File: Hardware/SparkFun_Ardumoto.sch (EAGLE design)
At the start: 33 parts, among them U1 ARDUINO, U2 L298, U3 74HC1G04, U4 74HC1G04

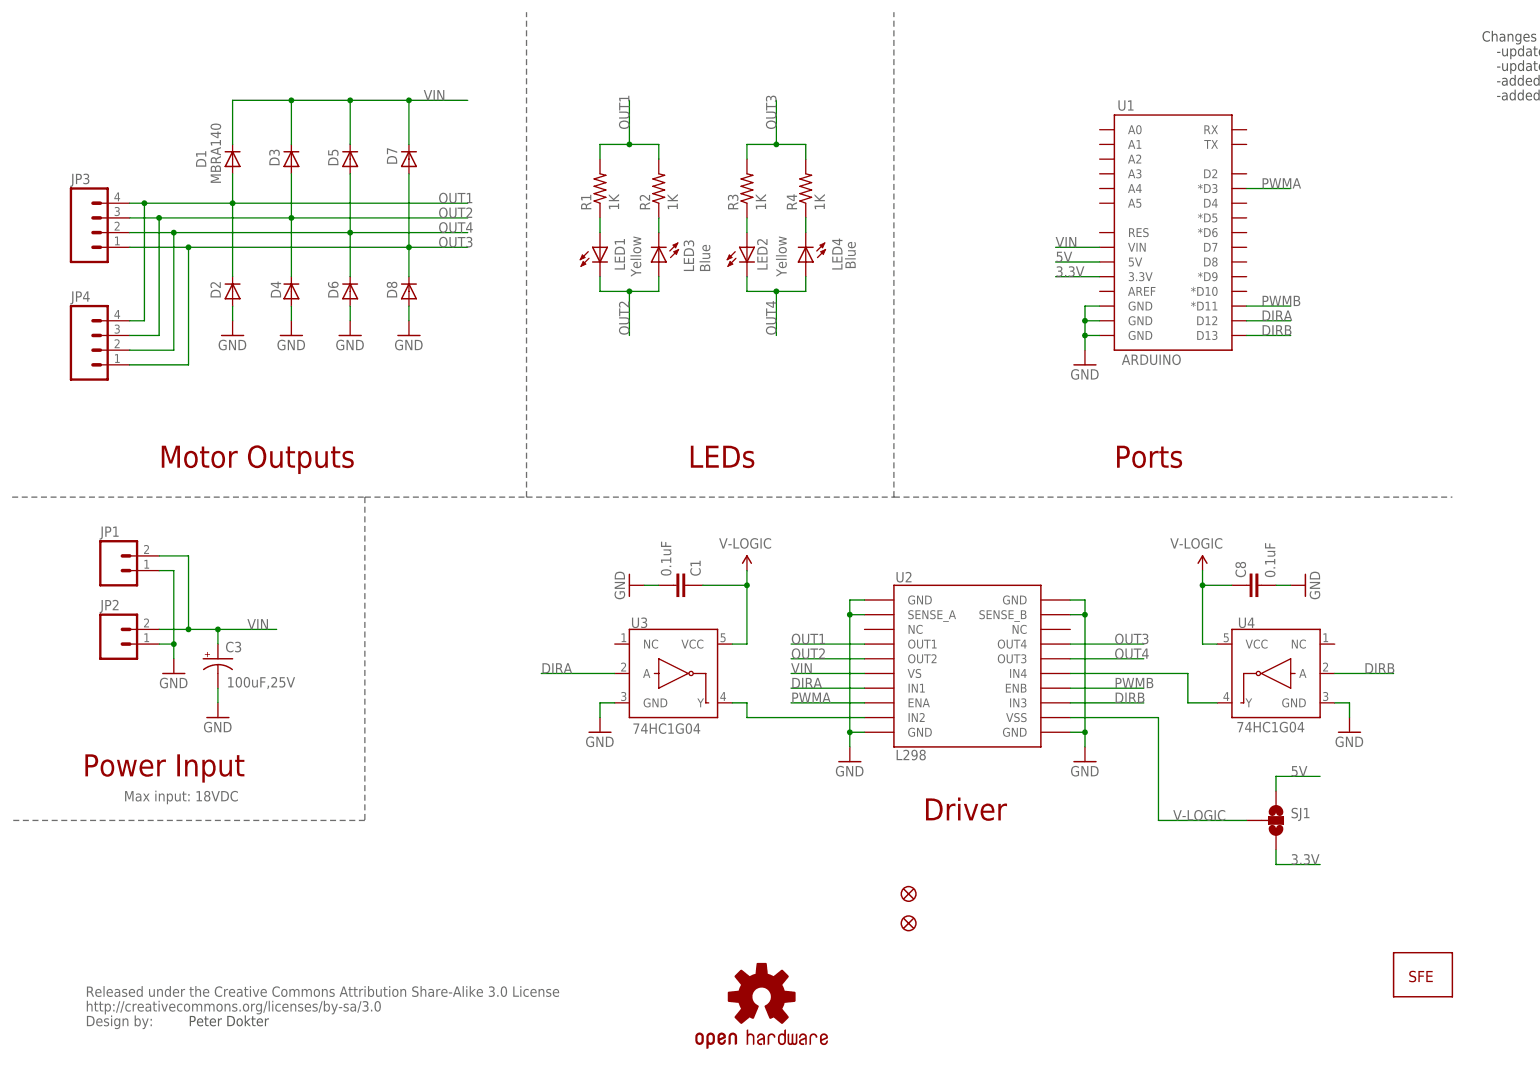
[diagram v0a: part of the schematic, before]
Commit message: Schematic is the same, but all parts have been updated to the new libraries.  The layout is no longer valid, and proto area has been moved aside.  This is ready for functional changes.
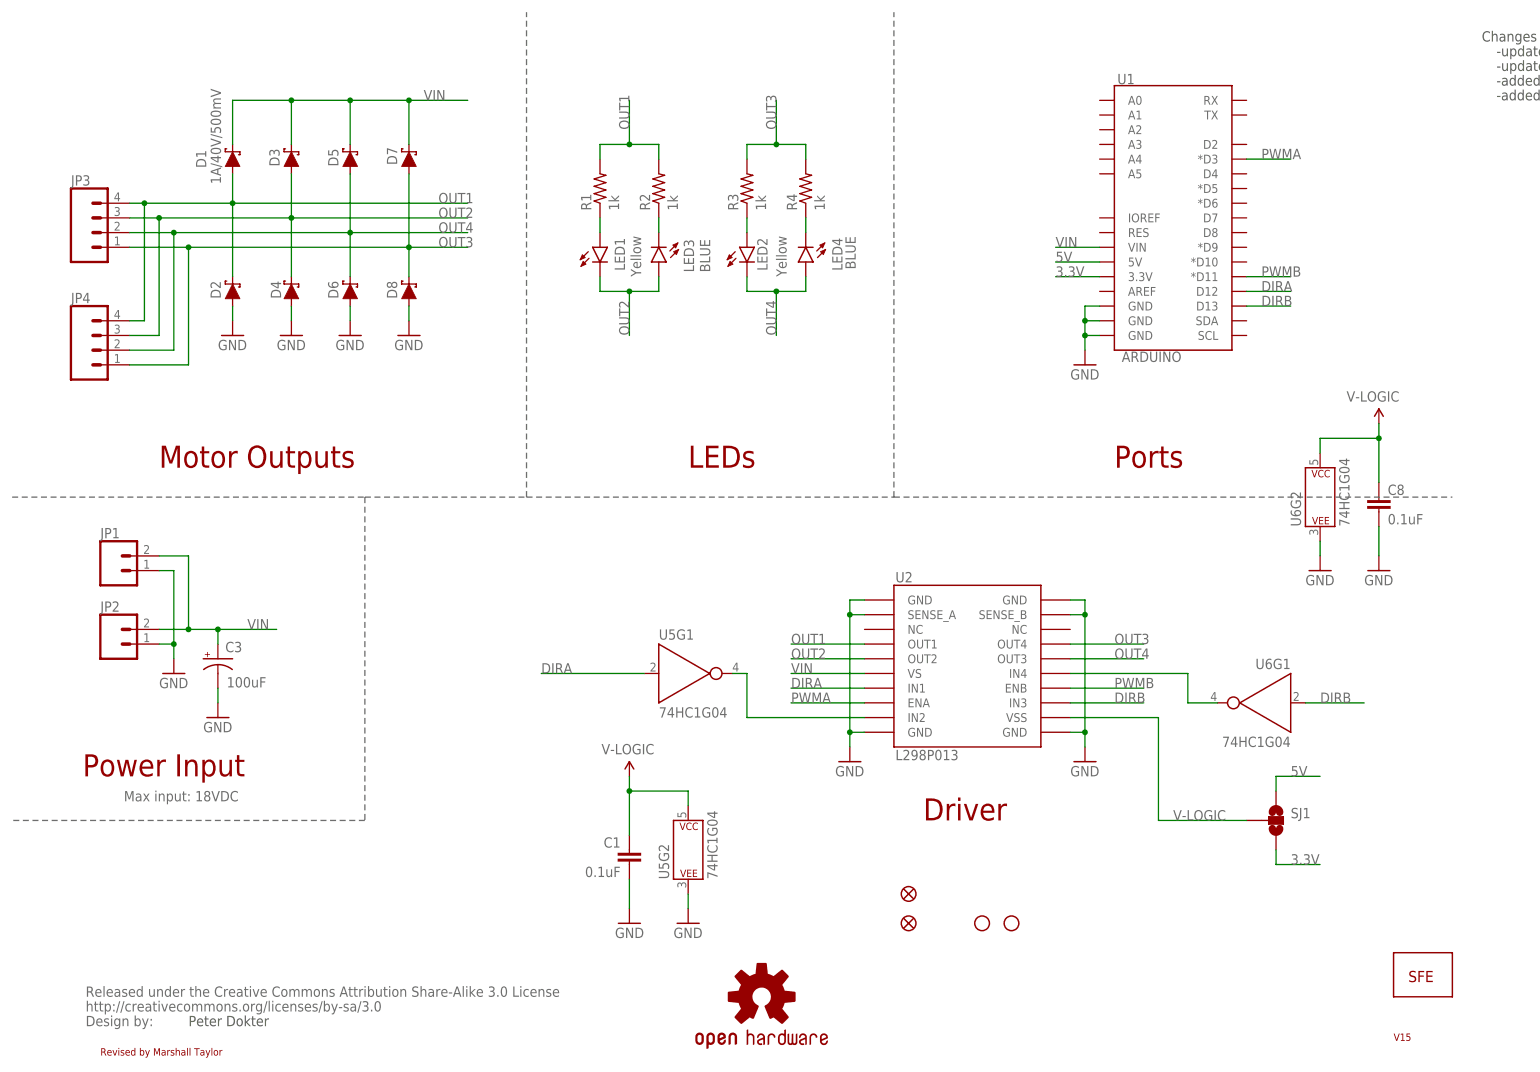
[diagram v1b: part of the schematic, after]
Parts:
- removed U3, U4: 74HC1G04, SparkFun:INVERTER""
- added H1, H2: STAND-OFF, SparkFun-Hardware:STAND-OFF
- added U5, U6: 74HC1G04, SparkFun-IC-Logic:74HC1G04
- C1, C8: device SparkFun:CAP0402-CAP -> SparkFun-Capacitors:0.1UF-0603-25V-5%
- C3: value 100uF,25V -> 100uF; device SparkFun:CAP_POLF80 -> SparkFun-Capacitors:100UF-POLAR-25V-20%(ELEC)
- D1, D2, D3, D4, D5, D6, D7, D8: value MBRA140 -> 1A/40V/500mV; device SparkFun:DIODESMA -> SparkFun-DiscreteSemi:DIODE-SCHOTTKY-SS14
- JP1: device SparkFun:M02PTH -> SparkFun-Connectors:CONN_02
- JP2: device SparkFun:M023.5MM -> SparkFun-Connectors:CONN_023.5MM
- JP3: device SparkFun:M04SCREW -> SparkFun-Connectors:CONN_04SCREW
- JP4: device SparkFun:M04PTH -> SparkFun-Connectors:CONN_04
- LED1, LED2: device SparkFun:LED0603 -> SparkFun-LED:LED-YELLOW0603
- LED3, LED4: value Blue -> BLUE; device SparkFun:LED0603 -> SparkFun-LED:LED-BLUE0603
- R1, R2, R3, R4: value 1K -> 1k; device SparkFun:RESISTOR0402-RES -> SparkFun-Resistors:1KOHM-0603-1/10W-1%
- U1: device SparkFun:ARDUINO_SHIELDNOLABELS -> SparkFun-Boards:ARDUINO_UNO_R3_SHIELDBASIC
- U2: value L298 -> L298P013; device SparkFun:L298_BRIDGE_DRIVER -> SparkFun-IC-Special-Function:L298_BRIDGE_DRIVER
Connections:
- net DIRA: now also U5G1.A; no longer U3.A
- net DIRB: now also U6G1.A; no longer U4.A
- net GND: now also U6G2.P$V-; no longer U3.GND, U4.GND
- net N$1: now also U5G1.Y; no longer U3.Y
- net N$2: now also U6G1.Y; no longer U4.Y
- net V-LOGIC: now also U6G2.P$V+; no longer U3.VCC, U4.VCC
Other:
- note added: "Revised by Marshall Taylor"
- note added: "V15"
- moved on the sheet: C1, C8

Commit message: Schematic changes applied, layout is now mostly ripped up
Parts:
- removed SJ1: (no value), SparkFun:SOLDERJUMPER_2WAYPASTE1&2
- added D10, D11, D12, D9: RED, SparkFun-LED:LED-RED0603
- added J1: (no value), SparkFun-Connectors:CONN_08NO_SILK_FEMALE_PTH
- added J2, J6: (no value), SparkFun-Connectors:CONN_01PTH_NO_SILK_YES_STOP
- added J3, J5: (no value), SparkFun-Connectors:CONN_06NO_SILK_FEMALE_PTH
- added J4: (no value), SparkFun-Connectors:CONN_07NO_SILK
- added J7, J8: (no value), SparkFun-Connectors:CONN_021X02_NO_SILK
- added JP10, JP7, JP8, JP9: JUMPER-SMT_3_1-NC_TRACE_SILK, SparkFun-Jumpers:JUMPER-SMT_3_1-NC_TRACE_SILK
- added JP11, JP12: JUMPER-SMT_2_NC_TRACE_SILK, SparkFun-Jumpers:JUMPER-SMT_2_NC_TRACE_SILK
- added R5, R6, R7, R8: 1k, SparkFun-Resistors:1KOHM-0603-1/10W-1%
- U1: device SparkFun-Boards:ARDUINO_UNO_R3_SHIELDBASIC -> SparkFun-Boards:ARDUINO_UNO_R3_SHIELDNOLABELS
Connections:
- net N$1 renamed IN2
- net N$2 renamed IN4
- removed net V-LOGIC: C1.1, C8.1, SJ1.2, U2.VSS, U6G2.P$V+
- new net D0: J1.1, U1.RX
- new net D1: J1.2, U1.TX
- new net D10: J5.3, JP10.1, U1.*D10
- new net D11: J5.4, U1.*D11
- new net D12: J5.5, U1.D12
- new net D13: J5.6, U1.D13
- new net D2: J1.3, JP7.1, U1.D2
- new net D3: J1.4, JP8.1, U1.*D3
- new net D4: J1.5, U1.D4
- new net D5: J1.6, JP9.3, U1.*D5
- new net D6: J1.7, JP9.1, U1.*D6
- new net D7: J1.8, JP7.3, U1.D7
- new net D8: J5.1, JP8.3, U1.D8
- new net D9: J5.2, JP10.3, U1.*D9
- new net IN1: J2.1, JP11.2, U2.IN1
- new net IN3: J6.1, JP12.1, U2.IN3
- new net IOREF: J4.7, U1.IOREF
- new net N$11: J8.2, U2.SENSE_B
- new net N$14: J7.1, U2.SENSE_A
- new net N$21: J3.1, U1.A0
- new net N$22: J3.2, U1.A1
- new net N$23: J3.3, U1.A2
- new net N$24: J3.4, U1.A3
- new net N$25: J3.5, U1.A4
- new net N$26: J3.6, U1.A5
- new net N$36: D9.A, R5.1
- new net N$37: D10.A, R6.1
- new net N$38: D12.A, R8.1
- new net N$39: D11.A, R7.1
- new net RESET: J4.6, U1.RES
- net 3.3V: now also J4.5; no longer SJ1.3
- net 5V: now also C1.1, C8.1, J4.4, U2.VSS, U5G2.P$V+, U6G2.P$V+; no longer SJ1.1
- net DIRA: now also JP11.1, JP8.2, R7.2; no longer U1.D12, U2.IN1
- net DIRB: now also JP12.2, JP7.2, R8.2; no longer U1.D13, U2.IN3
- net GND: now also D10.C, D11.C, D12.C, D9.C, J4.2, J4.3, J7.2, J8.1, U5G2.P$V-; no longer U2.SENSE_A, U2.SENSE_B
- net PWMA: now also JP9.2, R6.2; no longer U1.*D3
- net PWMB: now also JP10.2, R5.2; no longer U1.*D11
- net VIN: now also J4.1
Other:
- moved on the sheet: C1, C3, C8, D1, D2, D3, D4, D5, D6, D7, D8, JP1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

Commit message: Desing ready for proto 1 review
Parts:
- removed JP11, JP12: JUMPER-SMT_2_NC_TRACE_SILK, SparkFun-Jumpers:JUMPER-SMT_2_NC_TRACE_SILK
- removed U$10: LOGO-SFENEW, SparkFun:LOGO-SFENEW
- removed U$11: CREATIVE_COMMONS, SparkFun:CREATIVE_COMMONS
- added FD1, FD2: FIDUCIALUFIDUCIAL, SparkFun:FIDUCIALUFIDUCIAL
- added FRAME1: FRAME-LETTER, SparkFun-Aesthetics:FRAME-LETTER
- added FRAME2: FRAME-LETTERNO_PACKAGE, SparkFun-Aesthetics:FRAME-LETTERNO_PACKAGE
- added J10: (no value), SparkFun-Connectors:CONN_023.5MM
- added J11, J12, J13, J14: (no value), SparkFun-Connectors:CONN_01PTH_NO_SILK_YES_STOP
- added J9: (no value), SparkFun-Connectors:CONN_02
- added LOGO1: SFE_LOGO_NAME_FLAME.2_INCH, SparkFun-Aesthetics:SFE_LOGO_NAME_FLAME.2_INCH
- added LOGO2: SFE_LOGO_NAME.1_INCH, SparkFun-Aesthetics:SFE_LOGO_NAME.1_INCH
- J7: device SparkFun-Connectors:CONN_021X02_NO_SILK -> SparkFun-Connectors:CONN_04SCREW
- J8: device SparkFun-Connectors:CONN_021X02_NO_SILK -> SparkFun-Connectors:CONN_04
- JP1: value (none) -> 31NCT; device SparkFun-Connectors:CONN_02 -> SparkFun-Jumpers:JUMPER-SMT_3_1-NC_TRACE_SILK
- JP10, JP9: value JUMPER-SMT_3_1-NC_TRACE_SILK -> (none); device SparkFun-Jumpers:JUMPER-SMT_3_1-NC_TRACE_SILK -> SparkFun-Connectors:CONN_021X02_NO_SILK
- JP2: value (none) -> 31NCT; device SparkFun-Connectors:CONN_023.5MM -> SparkFun-Jumpers:JUMPER-SMT_3_1-NC_TRACE_SILK
- JP3: value (none) -> 31NCT; device SparkFun-Connectors:CONN_04SCREW -> SparkFun-Jumpers:JUMPER-SMT_3_1-NC_TRACE_SILK
- JP4: value (none) -> 31NCT; device SparkFun-Connectors:CONN_04 -> SparkFun-Jumpers:JUMPER-SMT_3_1-NC_TRACE_SILK
- JP5, JP6: value FIDUCIALUFIDUCIAL -> 2NCT; device SparkFun:FIDUCIALUFIDUCIAL -> SparkFun-Jumpers:JUMPER-SMT_2_NC_TRACE_SILK
- JP7, JP8: value JUMPER-SMT_3_1-NC_TRACE_SILK -> 2NCT; device SparkFun-Jumpers:JUMPER-SMT_3_1-NC_TRACE_SILK -> SparkFun-Jumpers:JUMPER-SMT_2_NC_TRACE_SILK
- U2: value L298P013 -> L298; device SparkFun-IC-Special-Function:L298_BRIDGE_DRIVER -> SparkFun-IC-Special-Function:L298_SMD_W_PAD
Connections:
- new net NDIRA: JP6.1, U5G1.Y
- new net NDIRB: JP7.2, U6G1.Y
- net D10: now also JP4.1; no longer JP10.1
- net D2: now also JP3.1; no longer JP7.1
- net D3: now also JP1.1; no longer JP8.1
- net D5: now also JP2.3; no longer JP9.3
- net D6: now also JP2.1; no longer JP9.1
- net D7: now also JP3.3; no longer JP7.3
- net D8: now also JP1.3; no longer JP8.3
- net D9: now also JP4.3; no longer JP10.3
- net DIRA: now also JP1.2, JP5.1; no longer JP11.1, JP8.2
- net DIRB: now also JP3.2, JP8.2; no longer JP12.2, JP7.2
- net GND: now also J10.1, J9.1, JP10.1, JP9.2, U2.GND@PAD; no longer J7.2, J8.1, JP1.1, JP2.1
- net IN1: now also JP5.2; no longer JP11.2
- net IN2: now also J14.1, JP6.2; no longer U5G1.Y
- net IN3: now also JP8.1; no longer JP12.1
- net IN4: now also J13.1, JP7.1; no longer U6G1.Y
- net N$11: now also JP10.2; no longer J8.2
- net N$14: now also JP9.1; no longer J7.1
- net N$8: now also LED4.C; no longer LED2.A
- net N$9: now also LED2.A; no longer LED4.C
- net OUT1: now also J7.4, J8.4; no longer JP3.4, JP4.4
- net OUT2: now also J7.3, J8.3; no longer JP3.3, JP4.3
- net OUT3: now also D5.A, D6.C, J7.2, J8.2, LED2.C, LED4.A, U2.OUT3; no longer D7.A, D8.C, JP3.1, JP4.1, R3.2, R4.2, U2.OUT4
- net OUT4: now also D7.A, D8.C, J7.1, J8.1, R3.2, R4.2, U2.OUT4; no longer D5.A, D6.C, JP3.2, JP4.2, LED2.C, LED4.A, U2.OUT3
- net PWMA: now also J11.1, JP2.2; no longer JP9.2
- net PWMB: now also J12.1, JP4.2; no longer JP10.2
- net VIN: now also J10.2, J9.2; no longer JP1.2, JP2.2
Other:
- note added: "All diode values are "1A/40V/500mV""
- note added: "BREAKOUT PINS: The following pins are not necessary for normal use but can be used for more specific operation J2, J13, J14, J11, J12, and J6 all connect to the driver's control pins, directly to the IC JP9 and JP10 are shorted in the layout, and can be split to apply current sense resistors to the A and B channels. JUMPERS: Open JP5 and JP6 before connecting to J2 and J14 for A-side totem drive 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"
- note added: "Drive LEDs"
- note added: "Driver Protection And Output"
- note added: "L298 Driver"
- note added: "Pete Dokter"
- note added: "Power Circuits"
- note added: "Power can be supplied through the Uno connection (not recommended), or by the screw/solder terminals on this shield. When supplying from the shield, current flows back to power the Uno. Only use one connection at a time. Max Vin voltage needs to be less than 18V"
- note added: "Revised by: Marshall Taylor"
- note added: "The folloing jumpers are used to set the ArduMoto's control pins to one of two possible connection points. Leave jumpers completely open if manually connecting control lines. JP1: 'A' Direction -- set to D8 (default) or D3 JP2: 'A' PWM signal -- set to D5 (default) or D6 JP3: 'B' Direction -- set to D7 (default) or D2 JP4: 'B' PWM signal -- set to D9 (default) or D10"
- note added: "Uno Pin Connection Jumpers"
- note added: "Uno R3 Connections"
- note added: "v15"
- note removed: "-added open source hardware logo"
- note removed: "-added version code to bottom copper"
- note removed: "-updated jumper footprint to improve reflow"
- note removed: "-updated to mirco-fiducial package"
- note removed: "Changes to v14 (5/29/2012)"
- note removed: "Driver"
- note removed: "LEDs"
- note removed: "Max input: 18VDC"
- note removed: "Motor Outputs"
- note removed: "Peter Dokter"
- note removed: "Ports"
- note removed: "Power Input"
- note removed: "Revised by Marshall Taylor"
- note removed: "V15"

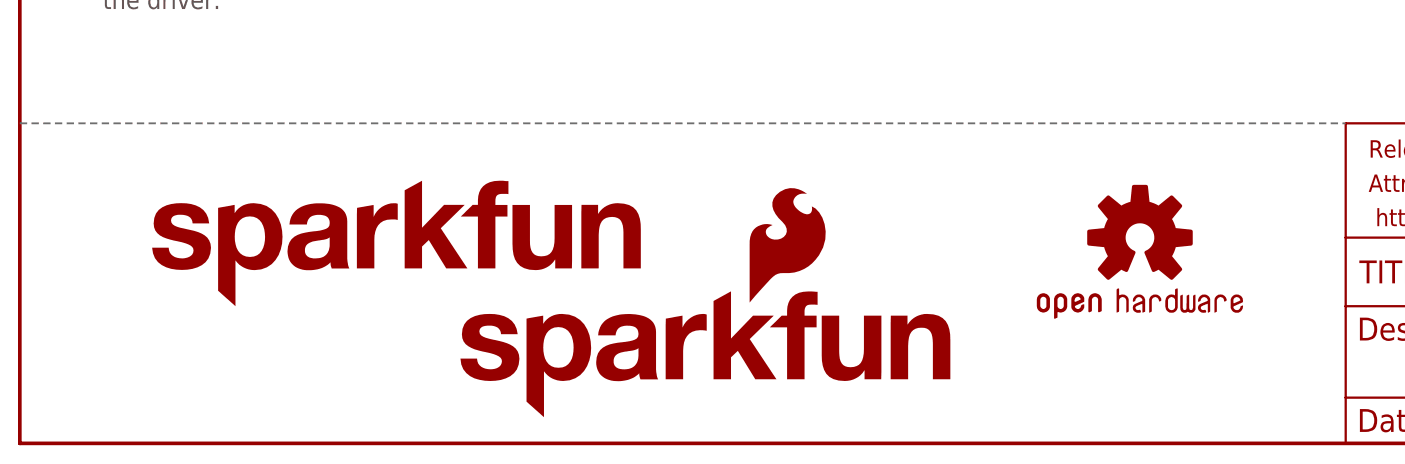
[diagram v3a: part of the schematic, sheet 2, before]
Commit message: Touched up the silk a bit in preparation for review
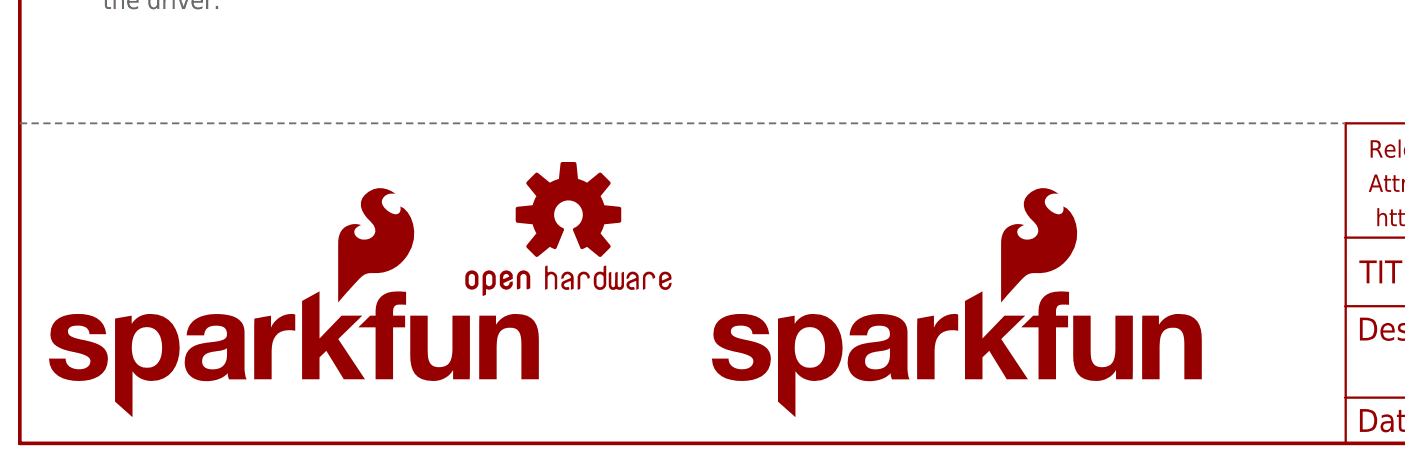
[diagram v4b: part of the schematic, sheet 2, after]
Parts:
- LOGO2: value SFE_LOGO_NAME.1_INCH -> SFE_LOGO_NAME_FLAME.1_INCH; device SparkFun-Aesthetics:SFE_LOGO_NAME.1_INCH -> SparkFun-Aesthetics:SFE_LOGO_NAME_FLAME.1_INCH
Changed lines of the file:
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@@
 <part name="JP7" library="SparkFun-Jumpers" deviceset="JUMPER-SMT_2_NC_TRACE" device="_SILK" value="2NCT"/>
 <part name="LOGO1" library="SparkFun-Aesthetics" deviceset="SFE_LOGO_NAME_FLAME" device=".2_INCH"/>
-<part name="LOGO2" library="SparkFun-Aesthetics" deviceset="SFE_LOGO_NAME" device=".1_INCH"/>
+<part name="LOGO2" library="SparkFun-Aesthetics" deviceset="SFE_LOGO_NAME_FLAME" device=".1_INCH"/>
 <part name="FRAME2" library="SparkFun-Aesthetics" deviceset="FRAME-LETTER" device="NO_PACKAGE"/>
 <part name="LED2" library="SparkFun-LED" deviceset="LED-YELLOW" device="0603" value="Yellow"/>
@@
 </instance>
 <instance part="SUPPLY4" gate="G$1" x="185.42" y="99.06" rot="MR0"/>
-<instance part="U$1" gate="G$1" x="124.46" y="22.86"/>
-<instance part="LOGO1" gate="G$1" x="48.26" y="2.54"/>
-<instance part="LOGO2" gate="G$1" x="12.7" y="15.24"/>
+<instance part="U$1" gate="G$1" x="60.96" y="25.4"/>
+<instance part="LOGO1" gate="G$1" x="76.2" y="2.54"/>
+<instance part="LOGO2" gate="G$1" x="2.54" y="2.54"/>
 <instance part="LED2" gate="G$1" x="223.52" y="144.78"/>
 <instance part="LED4" gate="G$1" x="213.36" y="142.24" rot="R180"/>

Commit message: Going for QC inspection
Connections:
- net N$11 renamed SENB
- net N$14 renamed SENA
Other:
- note added: "Power can be supplied through the Uno connection (not recommended), or by the screw/solder terminals on this shield. When supplying from the shield, current flows back to power the Uno. Only use one connection at a time. Vin range: 5V to 18V"
- note removed: "Power can be supplied through the Uno connection (not recommended), or by the screw/solder terminals on this shield. When supplying from the shield, current flows back to power the Uno. Only use one connection at a time. Max Vin voltage needs to be less than 18V"
- moved on the sheet: D1, D3, D5, D7, LED1, LED2, LED4, R1, R3, R4

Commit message: Reordered two R3 pins (9 and 6).  Switched sheet locations and adjusted logos.  Removed invalid airwires
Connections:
- net D10: now also JP4.3; no longer JP4.1
- net D5: now also JP2.1; no longer JP2.3
- net D6: now also JP4.1; no longer JP2.1
- net D9: now also JP2.3; no longer JP4.3
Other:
- note added: "The folloing jumpers are used to set the ArduMoto's control pins to one of two possible connection points. Leave jumpers completely open if manually connecting control lines. JP1: 'A' Direction -- set to D8 (default) or D3 JP2: 'A' PWM signal -- set to D9 (default) or D5 JP3: 'B' Direction -- set to D7 (default) or D2 JP4: 'B' PWM signal -- set to D10 (default) or D6"
- note removed: "The folloing jumpers are used to set the ArduMoto's control pins to one of two possible connection points. Leave jumpers completely open if manually connecting control lines. JP1: 'A' Direction -- set to D8 (default) or D3 JP2: 'A' PWM signal -- set to D5 (default) or D6 JP3: 'B' Direction -- set to D7 (default) or D2 JP4: 'B' PWM signal -- set to D9 (default) or D10"
